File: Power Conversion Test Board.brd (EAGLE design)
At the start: 136.7 x 125.3 mm, 48 parts, among them U1 LM2678, U2 LM2678

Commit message: Update Power Conversion Test Board.brd
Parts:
- moved C7 3.61 mm to (-118.9, 70.9), turned to 180 degrees
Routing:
- net +5V: track 0.00 -> 50.9 mm, vias 0 -> 1
- net 12VGND: track 0.00 -> 43.5 mm
- net +3.3V: track 0.00 -> 43.2 mm
- net 3.3VGND: track 5.41 -> 48.3 mm
- net +12V: track 44.3 -> 58.3 mm
- net N$10: track 0.00 -> 3.34 mm
- net 5VGND: track 49.8 -> 51.7 mm
- net +5V_3.3V: track 0.00 -> 1.70 mm
- added copper zone on layer 1, net +12V
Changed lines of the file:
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@@
 <attribute name="PROD_ID" value="CAP-00867" x="-98.044" y="68.326" size="1.778" layer="27" display="off"/>
 </element>
-<element name="C7" library="rcl" package="C0603" value="0.47uF" x="-116.078" y="73.152"/>
+<element name="C7" library="rcl" package="C0603" value="0.47uF" x="-118.872" y="70.866" rot="R180"/>
 <element name="J1" library="SparkFun-Connectors" library_urn="urn:adsk.eagle:library:513" package="BANANA_CONN" package3d_urn="urn:adsk.eagle:package:38018/1" value="" x="-142.24" y="83.82"/>
 <element name="J2" library="SparkFun-Connectors" library_urn="urn:adsk.eagle:library:513" package="BANANA_CONN" package3d_urn="urn:adsk.eagle:package:38018/1" value="" x="-143.51" y="74.168"/>
@@
 <wire x1="-119.298" y1="96.012" x2="-119.298" y2="90.17" width="1.27" layer="1"/>
 <wire x1="-119.298" y1="90.17" x2="-119.298" y2="84.328" width="1.27" layer="1"/>
-<wire x1="-119.298" y1="78.486" x2="-116.928" y2="73.152" width="0" layer="19" extent="1-1"/>
-<wire x1="-119.298" y1="84.328" x2="-119.298" y2="78.486" width="0" layer="19" extent="1-1"/>
-<wire x1="-98.044" y1="64.2112" x2="-116.928" y2="73.152" width="0" layer="19" extent="1-1"/>
+<wire x1="-119.298" y1="84.328" x2="-119.298" y2="78.486" width="1.27" layer="1"/>
+<polygon width="1.27" layer="1">
+<vertex x="-117.602" y="98.552"/>
+<vertex x="-121.92" y="98.552"/>
+<vertex x="-127.508" y="92.964"/>
+<vertex x="-127.508" y="83.058"/>
+<vertex x="-121.412" y="76.962"/>
+<vertex x="-117.602" y="76.962"/>
+</polygon>
+<wire x1="-119.298" y1="78.486" x2="-119.298" y2="74.34" width="1.27" layer="1"/>
+<wire x1="-118.022" y1="73.064" x2="-118.022" y2="70.866" width="1.27" layer="1"/>
+<wire x1="-119.298" y1="74.34" x2="-118.022" y2="73.064" width="1.27" layer="1"/>
+<wire x1="-118.022" y1="70.866" x2="-98.044" y2="64.2112" width="0" layer="19" extent="1-1"/>
 <wire x1="-73.578" y1="57.912" x2="-98.044" y2="64.2112" width="0" layer="19" extent="1-16"/>
 <wire x1="-69.762" y1="62.23" x2="-73.578" y2="57.912" width="0" layer="19" extent="16-16"/>
@@
 <contactref element="C12" pad="+"/>
 <contactref element="J6" pad="P$1"/>
+<via x="-92.71" y="101.346" extent="1-16" drill="0.35"/>
+<wire x1="-92.71" y1="101.346" x2="-87.884" y2="101.346" width="1.27" layer="1"/>
+<wire x1="-84.246" y1="97.708" x2="-84.246" y2="96.012" width="1.27" layer="1"/>
+<wire x1="-87.884" y1="101.346" x2="-84.246" y2="97.708" width="1.27" layer="1"/>
+<wire x1="-125.73" y1="112.014" x2="-121.158" y2="107.442" width="1.27" layer="16"/>
+<wire x1="-121.158" y1="107.442" x2="-121.158" y2="104.394" width="1.27" layer="16"/>
+<wire x1="-121.158" y1="104.394" x2="-118.11" y2="101.346" width="1.27" layer="16"/>
+<wire x1="-118.11" y1="101.346" x2="-92.71" y2="101.346" width="1.27" layer="16"/>
 <wire x1="-103.124" y1="64.2112" x2="-83.312" y2="42.252" width="0" layer="19" extent="1-1"/>
 <wire x1="-84.246" y1="84.328" x2="-103.124" y2="64.2112" width="0" layer="19" extent="1-1"/>
 <wire x1="-84.246" y1="90.17" x2="-84.246" y2="84.328" width="0" layer="19" extent="1-1"/>
 <wire x1="-84.246" y1="96.012" x2="-84.246" y2="90.17" width="0" layer="19" extent="1-1"/>
-<wire x1="-125.73" y1="112.014" x2="-84.246" y2="96.012" width="0" layer="19" extent="1-1"/>
 </signal>
 <signal name="N$1">
@@
 <contactref element="U$4" pad="P$4"/>
 <contactref element="J5" pad="P$1"/>
-<wire x1="-89.662" y1="33.146" x2="-108.966" y2="11.684" width="0" layer="19" extent="16-16"/>
-<wire x1="-79.788" y1="29.132" x2="-89.662" y2="33.146" width="0" layer="19" extent="16-16"/>
+<wire x1="-79.788" y1="29.132" x2="-81.964" y2="29.132" width="0.762" layer="16"/>
+<wire x1="-85.978" y1="33.146" x2="-89.662" y2="33.146" width="0.762" layer="16"/>
+<wire x1="-81.964" y1="29.132" x2="-85.978" y2="33.146" width="0.762" layer="16"/>
+<wire x1="-89.662" y1="33.146" x2="-91.568" y2="33.146" width="0.762" layer="16"/>
+<wire x1="-93.472" y1="31.242" x2="-93.472" y2="25.4" width="0.762" layer="16"/>
+<wire x1="-93.472" y1="25.4" x2="-107.188" y2="11.684" width="0.762" layer="16"/>
+<wire x1="-107.188" y1="11.684" x2="-108.966" y2="11.684" width="0.762" layer="16"/>
+<wire x1="-91.568" y1="33.146" x2="-93.472" y2="31.242" width="0.762" layer="16"/>
 </signal>
 <signal name="N$2">
@@
 <contactref element="C2" pad="-"/>
 <wire x1="-45.72" y1="92.876" x2="-45.72" y2="87.464" width="0.889" layer="1"/>
-<wire x1="-89.662" y1="24.804" x2="-99.568" y2="7.62" width="0" layer="19" extent="16-16"/>
-<wire x1="-79.788" y1="27.432" x2="-89.662" y2="24.804" width="0" layer="19" extent="16-16"/>
-<wire x1="-69.188" y1="27.432" x2="-79.788" y2="27.432" width="0" layer="19" extent="16-16"/>
+<wire x1="-99.568" y1="7.62" x2="-99.568" y2="14.898" width="0.762" layer="16"/>
+<wire x1="-99.568" y1="14.898" x2="-89.662" y2="24.804" width="0.762" layer="16"/>
+<wire x1="-89.662" y1="24.804" x2="-85.178" y2="24.804" width="0.762" layer="16"/>
+<wire x1="-82.55" y1="27.432" x2="-79.788" y2="27.432" width="0.762" layer="16"/>
+<wire x1="-85.178" y1="24.804" x2="-82.55" y2="27.432" width="0.762" layer="16"/>
+<wire x1="-69.188" y1="27.432" x2="-79.788" y2="27.432" width="0.762" layer="16"/>
 <wire x1="-65.786" y1="65.8368" x2="-69.188" y2="27.432" width="0" layer="19" extent="16-16"/>
 <wire x1="-65.786" y1="74.168" x2="-65.786" y2="65.8368" width="0" layer="19" extent="16-16"/>
@@
 <contactref element="R4" pad="2"/>
 <contactref element="C28" pad="C"/>
-<wire x1="-89.662" y1="29.846" x2="-89.662" y2="26.504" width="0" layer="19" extent="16-16"/>
+<wire x1="-89.662" y1="26.504" x2="-89.662" y2="29.846" width="0.762" layer="16"/>
 </signal>
 <signal name="+5V_3.3V">
@@
 <contactref element="U$4" pad="P$1"/>
 <contactref element="U$4" pad="P$2"/>
-<wire x1="-79.788" y1="25.732" x2="-79.788" y2="24.032" width="0" layer="19" extent="16-16"/>
-<wire x1="-68.326" y1="65.8368" x2="-79.788" y2="25.732" width="0" layer="19" extent="16-16"/>
+<wire x1="-79.788" y1="24.032" x2="-79.788" y2="25.732" width="0.762" layer="16"/>
+<wire x1="-79.788" y1="25.732" x2="-68.326" y2="65.8368" width="0" layer="19" extent="16-16"/>
 <wire x1="-66.376" y1="83.82" x2="-68.326" y2="65.8368" width="0" layer="19" extent="16-16"/>
 <wire x1="-66.376" y1="89.662" x2="-66.376" y2="83.82" width="0" layer="19" extent="16-16"/>
@@
 <vertex x="-93.472" y="99.06"/>
 </polygon>
-<wire x1="-115.228" y1="73.152" x2="-143.51" y2="74.168" width="0" layer="19" extent="1-1"/>
-<wire x1="-112.858" y1="78.486" x2="-115.228" y2="73.152" width="0" layer="19" extent="1-1"/>
-<wire x1="-112.858" y1="84.328" x2="-112.858" y2="78.486" width="0" layer="19" extent="1-1"/>
-<wire x1="-112.858" y1="90.17" x2="-112.858" y2="84.328" width="0" layer="19" extent="1-1"/>
-<wire x1="-112.858" y1="96.012" x2="-112.858" y2="90.17" width="0" layer="19" extent="1-1"/>
-<wire x1="-101.18" y1="72.644" x2="-112.858" y2="78.486" width="0" layer="19" extent="1-1"/>
-<wire x1="-101.174" y1="78.486" x2="-101.18" y2="72.644" width="0" layer="19" extent="1-1"/>
-<wire x1="-95.846" y1="72.644" x2="-95.93" y2="78.486" width="0" layer="19" extent="1-1"/>
+<wire x1="-112.858" y1="96.012" x2="-112.858" y2="90.17" width="1.27" layer="1"/>
+<wire x1="-112.858" y1="90.17" x2="-112.858" y2="84.328" width="1.27" layer="1"/>
+<wire x1="-112.858" y1="84.328" x2="-112.858" y2="78.486" width="1.27" layer="1"/>
+<polygon width="1.27" layer="1">
+<vertex x="-114.554" y="98.552"/>
+<vertex x="-114.554" y="76.708"/>
+<vertex x="-111.252" y="76.708"/>
+<vertex x="-111.252" y="98.552"/>
+</polygon>
+<wire x1="-143.51" y1="74.168" x2="-142.494" y2="75.184" width="1.27" layer="1"/>
+<wire x1="-142.494" y1="75.184" x2="-125.476" y2="75.184" width="1.27" layer="1"/>
+<wire x1="-121.158" y1="70.866" x2="-119.722" y2="70.866" width="1.27" layer="1"/>
+<wire x1="-125.476" y1="75.184" x2="-121.158" y2="70.866" width="1.27" layer="1"/>
+<wire x1="-112.858" y1="78.486" x2="-119.722" y2="70.866" width="0" layer="19" extent="1-1"/>
+<wire x1="-101.174" y1="96.012" x2="-112.858" y2="96.012" width="0" layer="19" extent="1-1"/>
+<wire x1="-101.18" y1="72.644" x2="-101.174" y2="78.486" width="0" layer="19" extent="1-1"/>
+<wire x1="-95.846" y1="72.644" x2="-101.18" y2="72.644" width="0" layer="19" extent="1-1"/>
 <wire x1="-100.584" y1="64.2112" x2="-101.18" y2="72.644" width="0" layer="19" extent="1-1"/>
 <wire x1="-100.584" y1="55.88" x2="-100.584" y2="64.2112" width="0" layer="19" extent="1-1"/>
@@
 <wire x1="-83.312" y1="46.902" x2="-83.312" y2="42.252" width="1.016" layer="16"/>
 <wire x1="-116.586" y1="119.888" x2="-116.586" y2="106.934" width="1.27" layer="1"/>
-<wire x1="-107.614" y1="97.962" x2="-107.614" y2="96.012" width="1.27" layer="1"/>
-<wire x1="-116.586" y1="106.934" x2="-107.614" y2="97.962" width="1.27" layer="1"/>
 <wire x1="-107.614" y1="96.012" x2="-107.614" y2="90.17" width="1.27" layer="1"/>
 <wire x1="-107.614" y1="90.17" x2="-107.614" y2="84.328" width="1.27" layer="1"/>
 <wire x1="-107.614" y1="84.328" x2="-107.614" y2="78.486" width="1.27" layer="1"/>
+<wire x1="-116.586" y1="106.934" x2="-116.586" y2="106.934" width="1.27" layer="1"/>
+<wire x1="-116.586" y1="106.934" x2="-116.586" y2="105.156" width="1.27" layer="1"/>
+<wire x1="-116.586" y1="105.156" x2="-112.776" y2="101.346" width="1.27" layer="1"/>
+<wire x1="-112.776" y1="101.346" x2="-109.474" y2="101.346" width="1.27" layer="1"/>
+<wire x1="-109.474" y1="101.346" x2="-107.614" y2="99.486" width="1.27" layer="1"/>
+<wire x1="-107.614" y1="99.486" x2="-107.614" y2="96.012" width="1.27" layer="1"/>
 <wire x1="-86.361" y1="60.944" x2="-83.312" y2="46.902" width="0" layer="19" extent="1-16"/>
 <wire x1="-90.931" y1="60.944" x2="-86.361" y2="60.944" width="0" layer="19" extent="1-1"/>

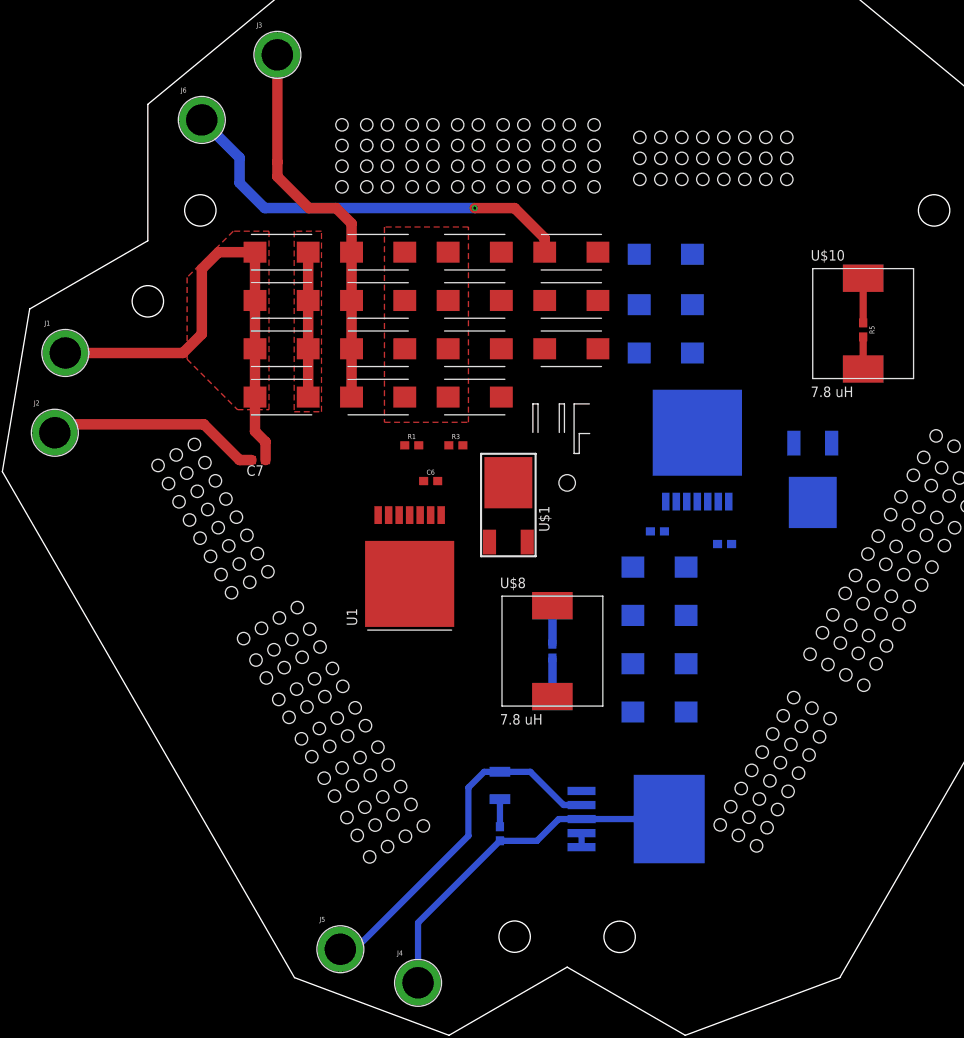
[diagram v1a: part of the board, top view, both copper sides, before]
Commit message: Replaced components and routed some more.
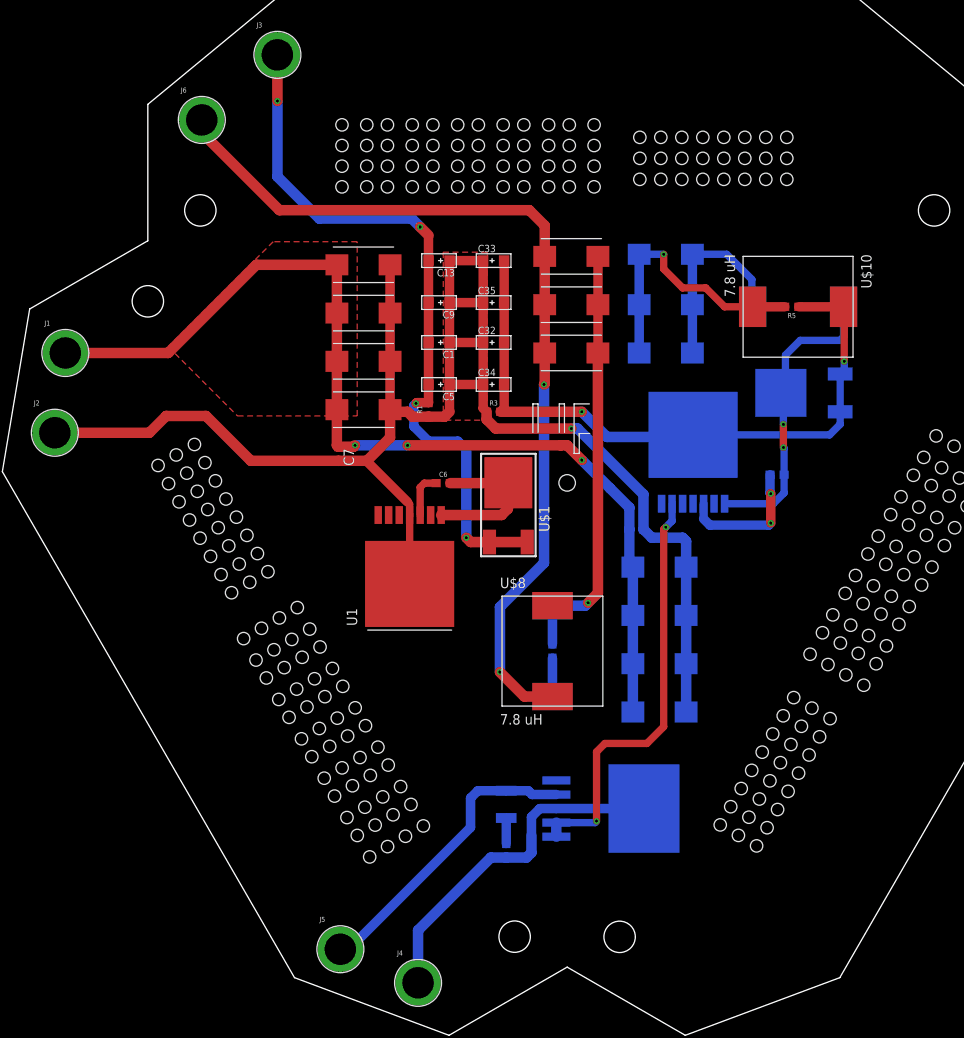
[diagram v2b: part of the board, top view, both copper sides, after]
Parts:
- removed C19, C27: 100uF, PowerComponents:CTAN(7.30_4.30MM)
- removed C2, C22: .1uF, PowerComponents:CTAN(7.30_4.30MM)
- removed C21: 10uF, PowerComponents:CTAN(7.30_4.30MM)
- removed C23, C4: .01uF, PowerComponents:CTAN(7.30_4.30MM)
- added C13, C35: .01uF, Seeed-Capacitor:AVX-A
- added C32, C5: 100uF, Seeed-Capacitor:AVX-A
- added C33: 10uF, Seeed-Capacitor:AVX-A
- added C34, C9: .1uF, Seeed-Capacitor:AVX-A
- C1: device PowerComponents:CTAN(7.30_4.30MM) -> Seeed-Capacitor:AVX-A
- moved C20 10.5 mm to (-56.1, 69.1)
- moved U$3 10.2 mm to (-52.6, 79.0), turned to 180 degrees
- moved C15 10.0 mm to (-106.2, 94.5)
- moved C16 10.0 mm to (-106.2, 88.6)
- moved C17 10.0 mm to (-106.2, 82.8)
- moved C18 10.0 mm to (-106.2, 77.0)
- moved C7 9.68 mm to (-109.2, 71.6), turned to 270 degrees
- moved R5 9.08 mm to (-54.4, 89.4), turned to 180 degrees
- moved U$10 8.13 mm to (-53.6, 89.4), turned to 270 degrees
- moved U$9 8.13 mm to (-53.6, 89.4), turned to 90 degrees
- moved R3 6.12 mm to (-90.4, 76.7)
- moved R1 4.77 mm to (-98.3, 77.0), turned to 90 degrees
- moved C1 4.38 mm to (-97.0, 85.1), turned to 180 degrees
- moved U$4 3.30 mm to (-72.1, 28.7)
- moved C3 2.55 mm to (-73.2, 62.5), turned to 180 degrees
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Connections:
- net 12VGND: now also C13.+, C32.+, C33.+, C34.+, C35.+, C5.+, C9.+; no longer C19.+, C2.+, C21.+, C22.+, C23.+, C27.+, C4.+
- net 3.3VGND: now also C32.-, C33.-, C34.-, C35.-; no longer C1.-, C19.-, C2.-, C4.-
- net 5VGND: now also C1.-, C13.-, C5.-, C9.-; no longer C21.-, C22.-, C23.-, C27.-
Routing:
- net 12VGND: track 43.5 -> 197.9 mm, vias 0 -> 1
- net 3.3VGND: track 48.3 -> 123.6 mm, vias 0 -> 2
- net +5V_3.3V: track 1.70 -> 75.5 mm, vias 0 -> 2
- net +12V: track 58.3 -> 122.7 mm, vias 0 -> 3
- net +5V: track 50.9 -> 111.5 mm, vias 1 -> 2
- net N$8: track 4.65 -> 51.5 mm, vias 0 -> 1
- net 5VGND: track 51.7 -> 91.1 mm, vias 0 -> 4
- net N$7: track 0.00 -> 36.6 mm, vias 0 -> 2
- net N$4: track 3.89 -> 33.2 mm, vias 0 -> 1
- net N$1: track 0.00 -> 18.5 mm
- net N$2: track 0.00 -> 16.3 mm, vias 0 -> 2
- net +3.3V: track 43.2 -> 36.3 mm
- net N$3: track 0.00 -> 5.51 mm

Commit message: the good stuffff
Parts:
- moved C24 1.92 mm to (-67.7, 96.0)
- moved C25 1.82 mm to (-67.8, 90.0)
- moved C26 1.82 mm to (-67.8, 84.2)
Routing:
- net 3.3VGND: track 123.6 -> 176.9 mm
- net +5V_3.3V: track 75.5 -> 109.1 mm, vias 2 -> 3
- net +5V: track 111.5 -> 133.6 mm, vias 2 -> 3
- net +12V: track 122.7 -> 142.7 mm, vias 3 -> 7
- net 5VGND: track 91.1 -> 109.7 mm, vias 4 -> 8
- net N$1: track 18.5 -> 35.1 mm
- net N$4: track 33.2 -> 29.0 mm
- net N$2: track 16.3 -> 15.6 mm
- added copper zone on layer 1, net +5V
- added copper zone on layer 16, net +5V_3.3V
- added copper zone on layer 1, net 5VGND
- added copper zone on layer 16, net 5VGND
- added copper zone on layer 16, net N$4
- added copper zone on layer 1, net N$8
